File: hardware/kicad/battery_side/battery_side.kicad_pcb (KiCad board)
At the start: 2 copper layers, 60 x 40 mm, 45 parts, among them J1 Conn_01x02, J2 RJ45, J3 USB-OTG, J5 UART-DBG, Q1 AO3401A, Q2 AO3400A, U1 TPS62933FDRLR, U2 R-78E12-1.0, U3 SN65HVD3082E

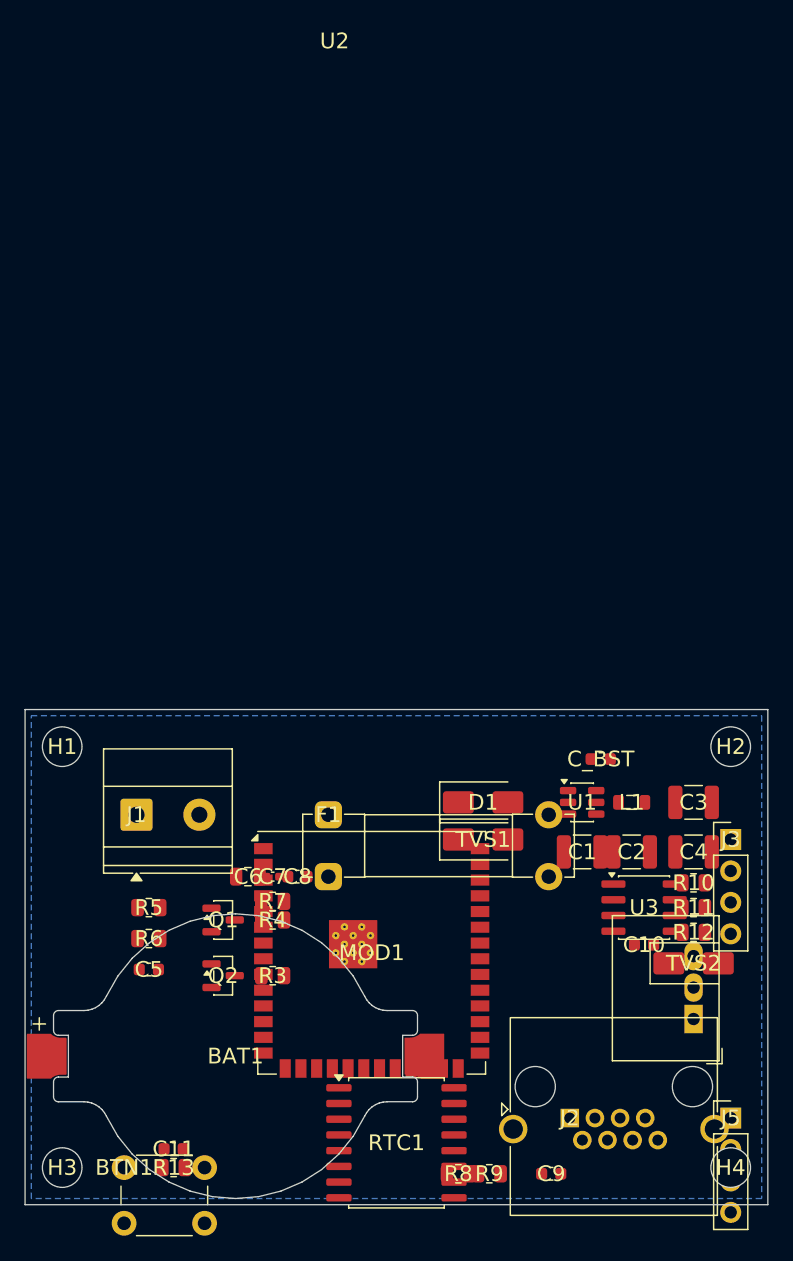
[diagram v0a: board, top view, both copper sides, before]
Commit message: hardware: CP5 iter-5 — both boards routed via Freerouting
Routing pipeline operational + reproducible:

build_pcbs.py:
- New _autoroute(pcb_path, board_name) helper. End-to-end: DSN
  export via pcbnew.ExportSpecctraDSN → Freerouting v1.9.0
  (defaults) → pcbnew.ImportSpecctraSES → ZONE_FILLER refill →
  SaveBoard. Stdin redirected from /dev/null to unblock v2's
  save-after-autoroute step.
- New --autoroute CLI flag; AUTOROUTE module-level flag toggles
  routing on per-board build invocations.

Board state:
- battery_side.kicad_pcb: 204 segments + 33 vias (Freerouting
  v2.1.0 -mp 300 -mt 1 -ic true; v1.9.0's optimizer phase hung
  indefinitely on this board, v2 with stdin /dev/null works).
  53 of 102 connections unrouted; DRC reports 0 unconnected
  items (all nets electrically connected, some via B.Cu pour).
- display_side.kicad_pcb: 289 segments + 44 vias (Freerouting
  v1.9.0 + JDK 21, defaults). 2 of 82 unrouted; DRC reports 0
  unconnected.

DRC outcomes:
- battery: 409 violations + 46 schematic parity (vs pre-route
  388 + 46 baseline; +21 from routing — 4 new errors total,
  rest warnings).
- display: 100 violations + 34 parity (vs pre-route 94 + 34;
  +6 from routing — 1 new error, 5 isolated_copper warnings).

D11 visual inspection — iter 5 evidence at
hardware/reviews/visual_inspections/cp5-routing-drc/iter5/ —
4 PNGs at 2k + 4 at 4k + MANIFEST.sha256. Packet §11.5 + §D11
iter 5 sections with sign-off scorecard.

SEMAPHORE stays claude_turn iter-5 — codex is offline; user
authorized 2-day solo session; iter-6 will drive routing-
introduced DRC errors to zero.

Co-Authored-By: Claude Opus 4.7 (1M context) <noreply@anthropic.com>
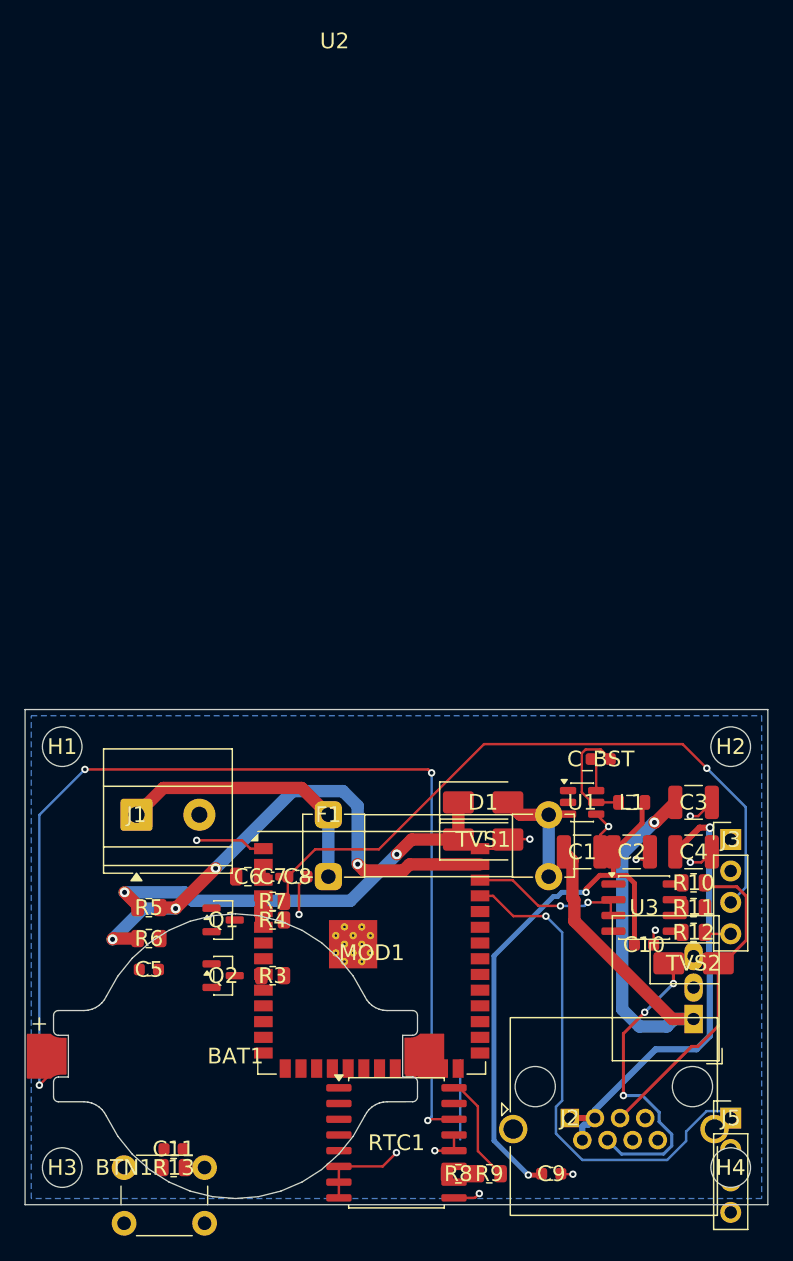
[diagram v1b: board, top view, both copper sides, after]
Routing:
- net V_BAT_RTC: track 0.00 -> 88.3 mm, vias 0 -> 4
- net ESP_EN: track 0.00 -> 53.9 mm, vias 0 -> 1
- net GND: track 0.00 -> 46.9 mm, vias 0 -> 12
- net V3V3_SW: track 0.00 -> 46.3 mm, vias 0 -> 2
- net V24_SW: track 0.00 -> 44.0 mm, vias 0 -> 1
- net V24_SENSE: track 0.00 -> 43.6 mm, vias 0 -> 4
- net DBG_UART_TX: track 0.00 -> 41.6 mm, vias 0 -> 1
- net V12_CAT5E: track 0.00 -> 38.7 mm, vias 0 -> 1
- net V24_FUSED: track 0.00 -> 34.0 mm, vias 0 -> 2
- net RS485_B: track 0.00 -> 26.5 mm
- net RS485_A: track 0.00 -> 25.0 mm, vias 0 -> 3
- net V24_RAW: track 0.00 -> 22.3 mm
- net DE_RE: track 0.00 -> 13.0 mm, vias 0 -> 2
- net U1_SW: track 0.00 -> 9.21 mm
- net I2C_SCL: track 0.00 -> 8.75 mm
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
